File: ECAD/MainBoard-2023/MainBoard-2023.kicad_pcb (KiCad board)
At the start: 2 copper layers, 60 x 150 mm, 69 parts, among them J1 XT60, J10 Conn_01x14, J11 Conn_01x03, J12 Conn_01x04, J13 Conn_01x03, J14 Conn_01x03, J15 Conn_01x03, J2 Conn_01x04, J20 BAU, J21 BAU, J22 Conn_01x04, J23 Conn_01x02, J24 Conn_01x07, J26 BAU, J27 BAU, J28 Conn_01x02, J29 Conn_01x02, J3 ConStep1, J30 Conn_01x03, J32 Conn_01x02, J37 Conn_01x02, J38 Conn_01x02, J39 Conn_01x02, J4 Conn_01x02, J40 Conn_01x02, J5 ConStep1, J6 ConStep1, J7 XT30, J8 Conn_01x02, J9 XT60, K1 CB1-P-24V, U1 Teensy3.5_All_Pins, U2 R-78B3.3-2.0, U4 R-78B5.0-2.0

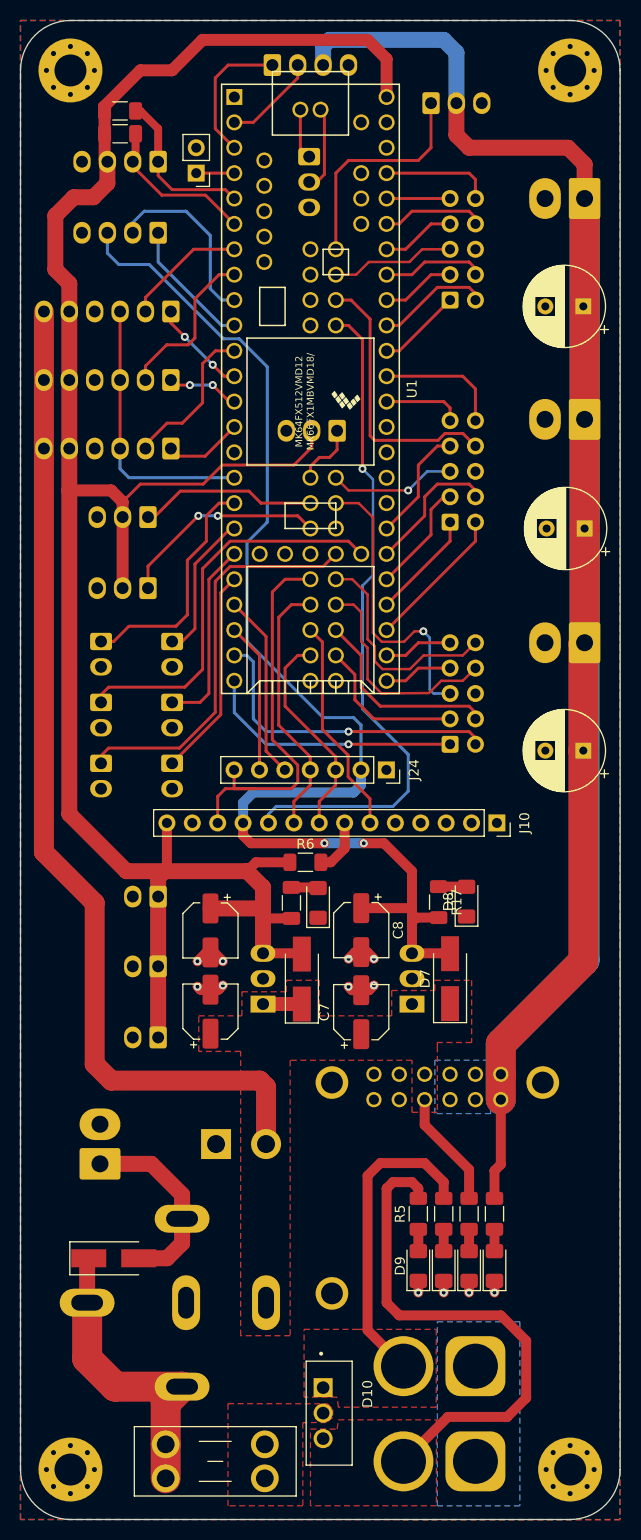
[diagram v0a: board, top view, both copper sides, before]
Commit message: add connectors - modify pinout
add 3 power connectors XT-30 24V
modify pinout to have a minimum of 2 pwm for each sattellite connectors
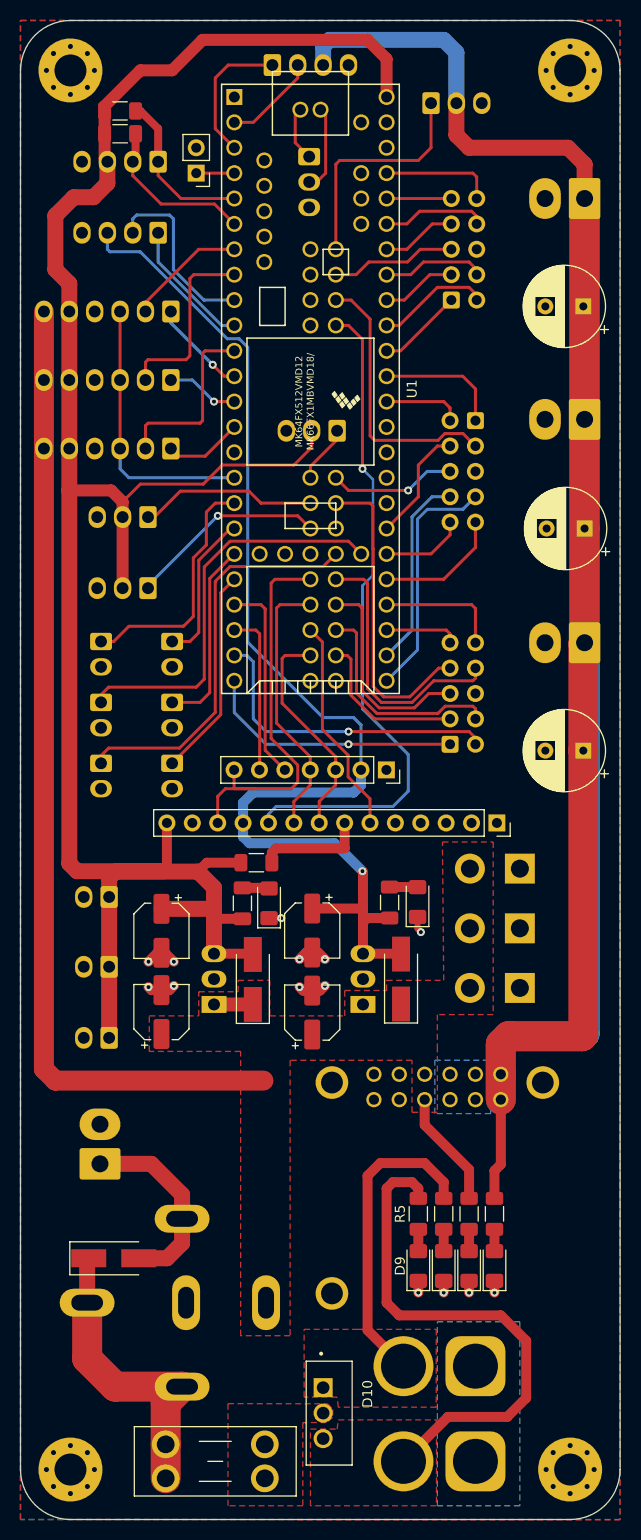
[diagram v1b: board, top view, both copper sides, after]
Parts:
- added J16: XT30, Connector_AMASS:AMASS_XT30UPB-F_1x02_P5.0mm_Vertical, B.Cu at (141.0, 110.9)
- added J17: XT30, Connector_AMASS:AMASS_XT30UPB-F_1x02_P5.0mm_Vertical, B.Cu at (141.0, 116.8)
- J22: value Conn_01x04 -> I2C
- moved J7 34.2 mm to (141.0, 122.8), turned to 180 degrees
- moved C_Act2 10.5 mm to (136.5, 66.0), turned to 180 degrees
- moved D2 4.90 mm to (114.3, 122.0)
- moved D7 4.90 mm to (129.1, 121.9)
- moved R17 4.90 mm to (127.9, 114.3)
- moved U2 4.90 mm to (125.3, 124.5)
- moved C1 4.90 mm to (105.1, 125.2)
- moved C2 4.90 mm to (105.1, 117.1)
- moved C7 4.90 mm to (120.2, 125.3)
- moved C8 4.90 mm to (120.2, 117.1)
- moved D3 4.90 mm to (115.9, 114.3)
- moved J23 4.90 mm to (99.9, 120.7)
- moved J28 4.90 mm to (99.9, 127.8)
- moved J29 4.90 mm to (99.9, 113.7)
- moved R2 4.90 mm to (113.2, 114.3)
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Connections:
- C_Act2 pad 1: C_Act2-1 -> C_Act2-8
- C_Act2 pad 10: C_Act2-8 -> C_Act2-1
- C_Act2 pad 2: C_Act2-2 -> C_Act2-7
- C_Act2 pad 3: C_Act2-3 -> C_Act2-6
- C_Act2 pad 4: C_Act2-4 -> C_Act2-5
- C_Act2 pad 5: C_Act2-9 -> GND
- C_Act2 pad 6: GND -> C_Act2-9
- C_Act2 pad 7: C_Act2-5 -> C_Act2-4
- C_Act2 pad 8: C_Act2-6 -> C_Act2-3
- C_Act2 pad 9: C_Act2-7 -> C_Act2-2
- U1 pad 30: C_Act3-5 -> C_Act2-4
- U1 pad 31: C_Act3-7 -> C_Act2-3
- U1 pad 32: C_Act2-2 -> C_Act3-7
- U1 pad 33: C_Act2-1 -> C_Act3-8
- U1 pad 34: C_Act2-3 -> C_Act2-2
- U1 pad 35: C_Act2-4 -> C_Act2-1
- U1 pad 78: C_Act3-6 -> C_Act3-9
- U1 pad 79: C_Act3-8 -> C_Act3-6
- U1 pad 81: C_Act3-9 -> C_Act3-5
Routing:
- net C_Act3-5: track 6.88 -> 31.2 mm
- net C_Act2-4: track 13.8 -> 24.2 mm
- net C_Act3-8: track 22.3 -> 12.5 mm
- net C_Act3-9: track 30.0 -> 21.2 mm, vias 1 -> 0
- net +5VP: track 239.2 -> 247.7 mm
- net C_Act2-3: track 11.3 -> 19.6 mm
- net +3V3: track 126.2 -> 119.4 mm, vias 2 -> 1
- net Net-(J10-Pad7): track 5.50 -> 11.0 mm
- net C_Act3-6: track 22.2 -> 27.3 mm
- net +24V: track 116.8 -> 113.9 mm
- net +5V: track 215.7 -> 218.6 mm
- net GND: track 16.8 -> 19.6 mm, vias 12 -> 14
- net STEP_3: track 15.5 -> 18.2 mm
- net C_Act3-4: track 19.9 -> 22.4 mm
- net C_Act2-1: track 10.9 -> 8.41 mm
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
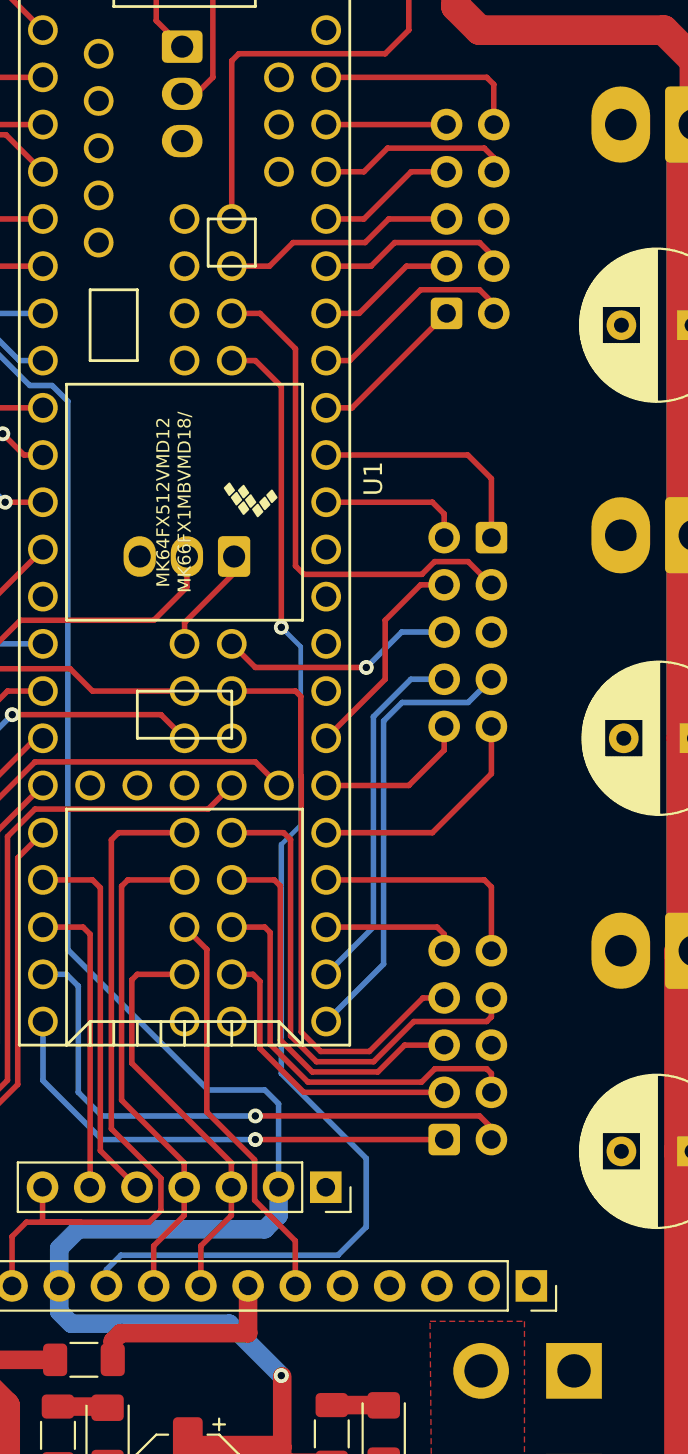
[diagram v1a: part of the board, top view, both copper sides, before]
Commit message: Change Pinout
Change pinout for the Satellite connectors
- 2 PWM
- 4 analog
- 3 other (mix digital/analog/pwm depending on the connector)
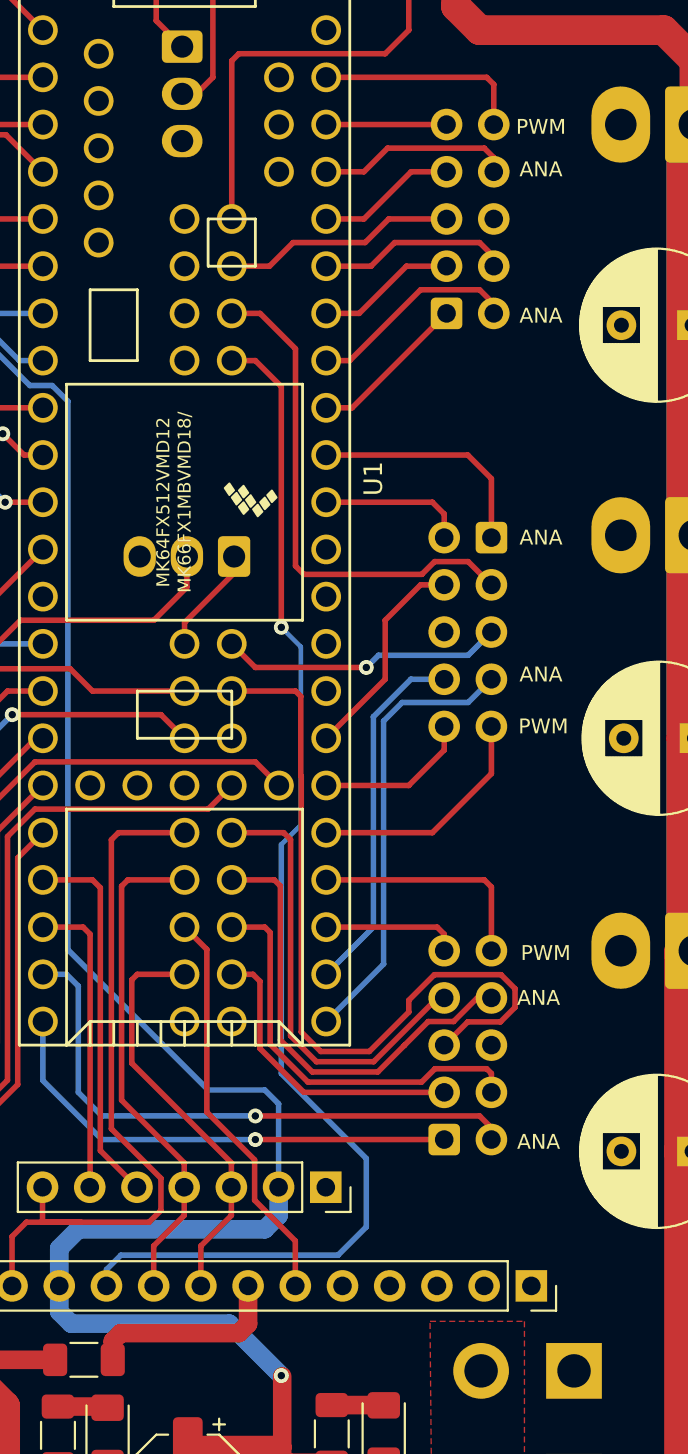
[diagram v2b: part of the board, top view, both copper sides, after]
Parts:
- J22: value I2C -> Conn_01x04
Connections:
- C_Act2 pad 5: GND -> C_Act2-9
- C_Act2 pad 6: C_Act2-9 -> GND
- U1 pad 78: C_Act3-9 -> C_Act3-6
- U1 pad 79: C_Act3-6 -> C_Act3-5
- U1 pad 81: C_Act3-5 -> C_Act3-9
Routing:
- net C_Act3-9: track 21.2 -> 41.9 mm
- net C_Act3-5: track 31.2 -> 24.1 mm
- net C_Act2-9: track 12.7 -> 15.3 mm
- net C_Act3-6: track 27.3 -> 24.8 mm
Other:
- board text added: "ANA"
- board text added: "PWM"

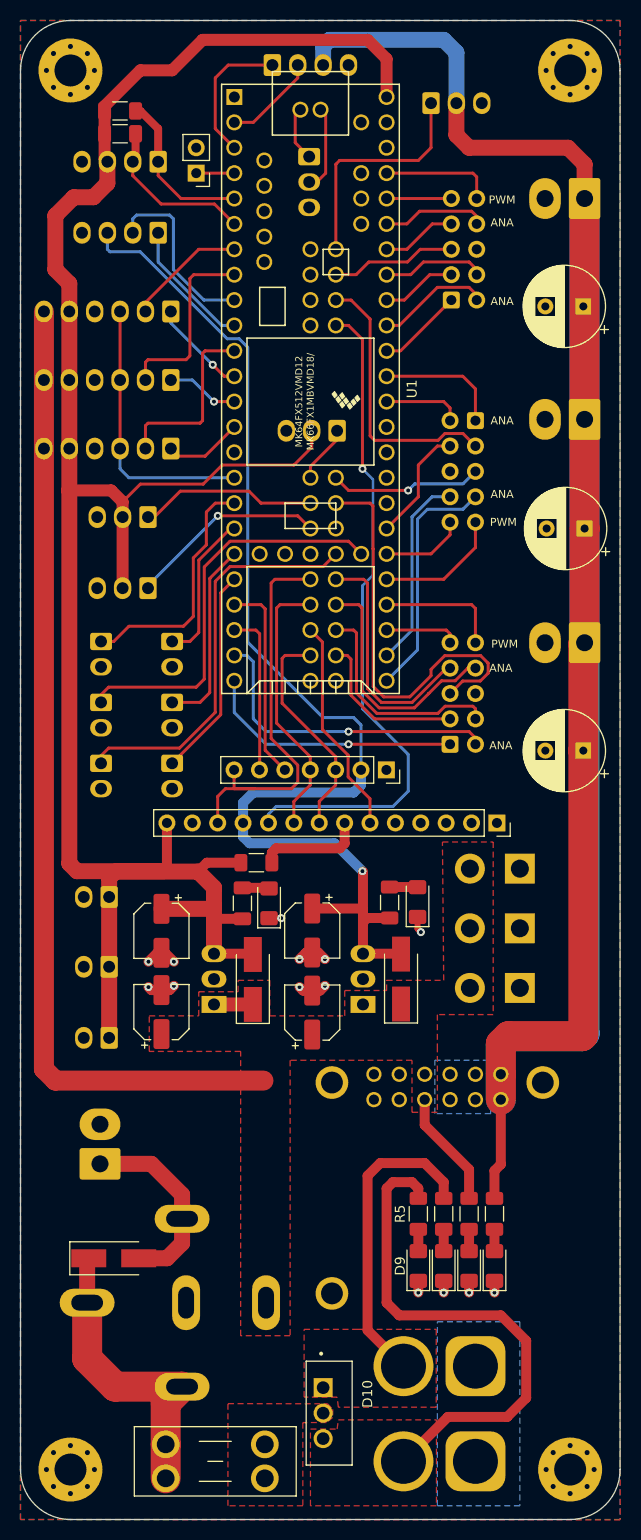
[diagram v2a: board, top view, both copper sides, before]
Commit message: clean PCB
Clean routing and DRC errors
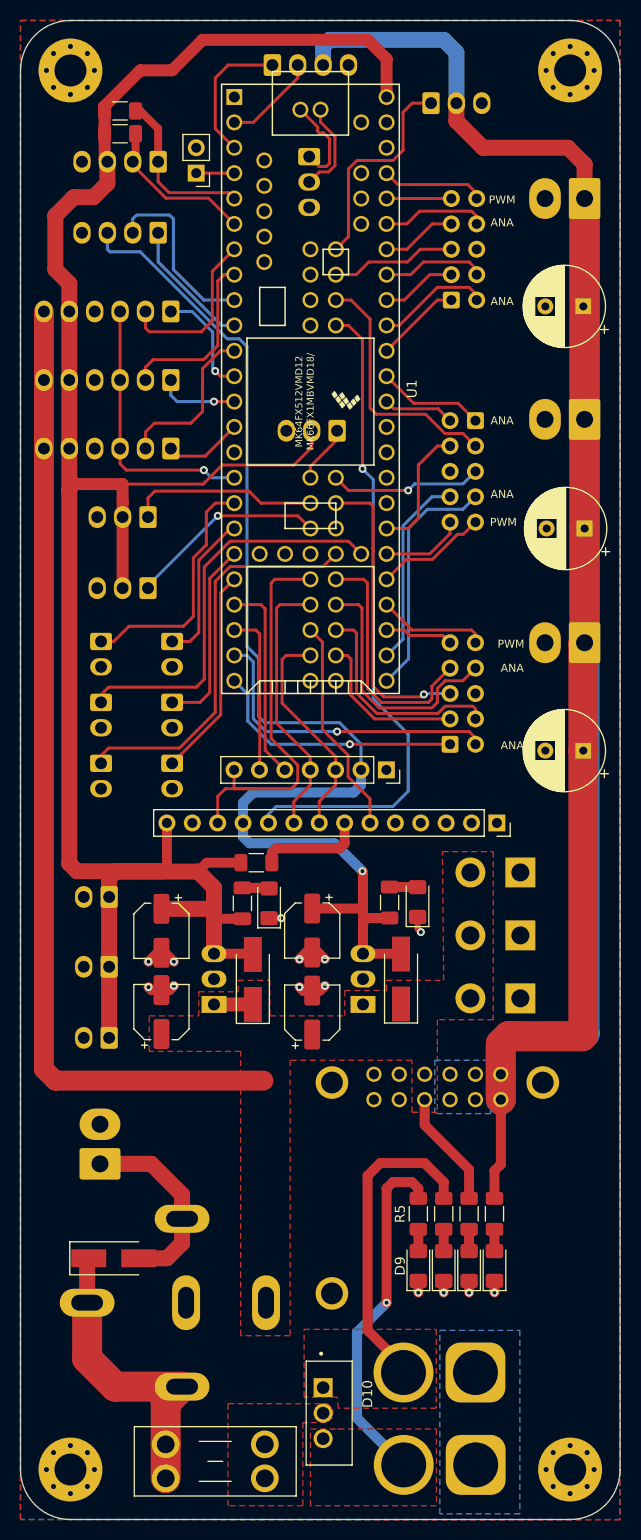
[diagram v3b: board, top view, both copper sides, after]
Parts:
- moved J7 1.04 mm to (141.0, 123.9)
- moved J17 0.71 mm to (141.0, 117.6)
- moved J1 0.63 mm to (136.5, 161.3)
- moved J16 0.38 mm to (141.0, 111.3)
- moved J9 0.36 mm to (136.6, 170.5)
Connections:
- net Net-(J15-Pad1) renamed /D+
- net Net-(J15-Pad2) renamed /D-
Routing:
- net ALIM: track 52.3 -> 35.5 mm, vias 0 -> 1
- net C_Act3-9: track 41.9 -> 30.2 mm, vias 0 -> 1
- net STEP_1: track 12.0 -> 17.0 mm
- net /D+: track 5.49 -> 9.46 mm
- net +3V3: track 119.4 -> 122.0 mm
- net C_Act2-6: track 27.4 -> 25.2 mm
- net C_Act2-8: track 12.6 -> 10.7 mm
- net STEP_3: track 18.2 -> 16.4 mm
- net +5V: track 218.6 -> 220.2 mm
- net C_Act3-8: track 12.5 -> 11.0 mm
- net C_Act2-2: track 12.7 -> 11.3 mm
- net DIR_1: track 9.70 -> 11.2 mm
- net NEO_PIXEL: track 23.2 -> 21.8 mm
- net C_Act2-5: track 11.6 -> 12.9 mm
- net Sensor-02: track 17.8 -> 18.9 mm
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
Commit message: Add silkscreen info
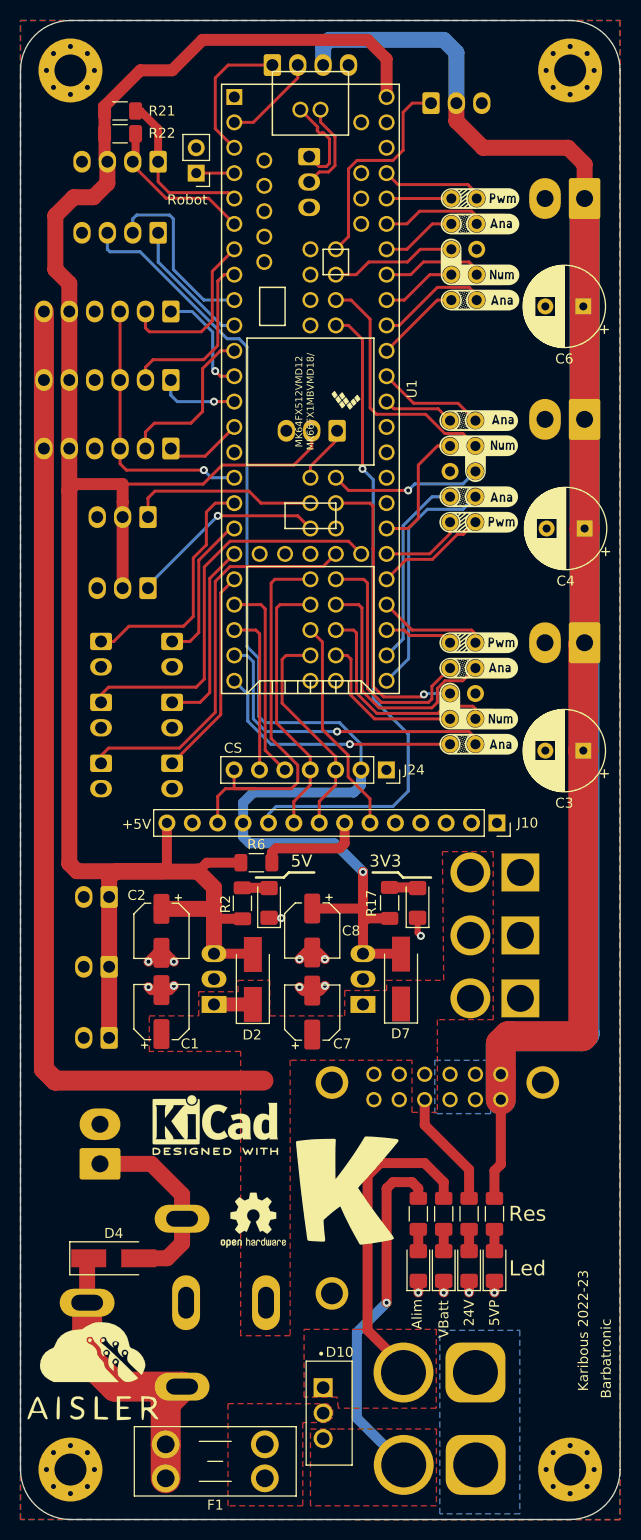
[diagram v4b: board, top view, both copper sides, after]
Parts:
- added G***: LOGO, LOGO, F.Cu at (137.0, 48.9)
- added G***: LOGO, aisler:aisler_15x12mm, F.Cu at (98.4, 161.3)
- added G***: LOGO, LOGO, F.Cu at (136.8, 71.1)
- added G***: LOGO, LOGO, F.Cu at (136.9, 93.3)
- added REF**: OSHW-Logo2_7.3x6mm_SilkScreen, Symbol:OSHW-Logo2_7.3x6mm_SilkScreen, F.Cu at (114.3, 146.1)
- added REF**: KiCad-Logo2_5mm_SilkScreen, Symbol:KiCad-Logo2_5mm_SilkScreen, F.Cu at (110.5, 136.5)
- J16, J17, J7: footprint Connector_AMASS:AMASS_XT30UPB-F_1x02_P5.0mm_Vertical -> Connector_AMASS:AMASS_XT30U-F_1x02_P5.0mm_Vertical
- moved D8 0.09 mm to (130.7, 114.3)
- renumbered F2 to F1
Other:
- board text added: "+5V"
- board text added: "24V"
- board text added: "3V3"
- board text added: "5V"
- board text added: "5VP"
- board text added: "Alim"
- board text added: "Barbatronic"
- board text added: "CS"
- board text added: "Karibous 2022-23"
- board text added: "Led"
- board text added: "Res"
- board text added: "Robot"
- board text added: "VBatt"
- board text removed: "ANA"
- board text removed: "PWM"

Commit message: add silkscreen elements
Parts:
- added G***: LOGO, LOGO, B.Cu at (106.1, 135.5)
- added G***: LOGO, LOGO, B.Cu at (114.9, 133.1)
- added G***: LOGO, LOGO, B.Cu at (144.3, 164.3)
- added G***: LOGO, LOGO, B.Cu at (98.4, 51.2)
- added kibuzzard-62E65D6B: G***, kibuzzard-62E65D6B, B.Cu at (108.8, 55.1)
- added kibuzzard-62E65D77: G***, kibuzzard-62E65D77, B.Cu at (109.0, 62.0)
- added kibuzzard-62E65D7D: G***, kibuzzard-62E65D7D, B.Cu at (109.0, 68.8)
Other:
- board text added: "+"
- board text added: "-"
- board text added: "3V3 Reg."
- board text added: "5V Reg."
- board text added: "Alim ext."
- board text added: "Arrêt d'urgence"
- board text added: "Batterie"
- board text added: "Detec"
- board text added: "Dir"
- board text added: "En"
- board text added: "Init"
- board text added: "Progr"
- board text added: "Reset"
- board text added: "Sensor 01"
- board text added: "Sensor 02"
- board text added: "Sensor 03"
- board text added: "St"
- board text added: "Team"
- board text added: "Tirette"
